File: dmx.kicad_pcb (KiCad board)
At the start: 2 copper layers, 73 x 99.4 mm, 115 parts, among them J1 Conn_01x15_Socket, J10 Conn_01x04_Pin, J11 USB_C_Receptacle_USB2.0_16P, J12 Conn_01x03_Pin, J13 XLR A/B, J14 Conn_01x04_Socket, J15 XLR3, J16 XLR3, J2 Conn_01x04_Pin, J3 Conn_01x15_Socket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

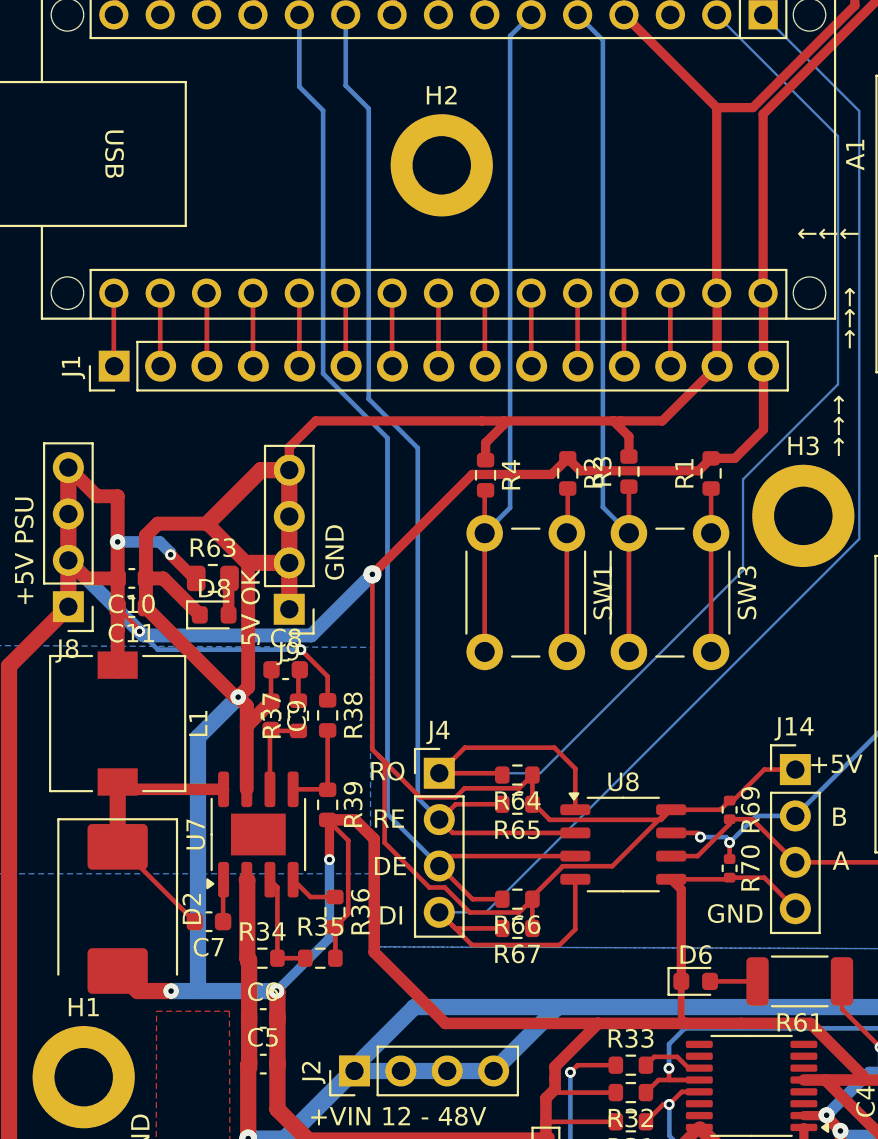
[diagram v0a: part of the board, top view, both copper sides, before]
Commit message: switch to cheaper components.
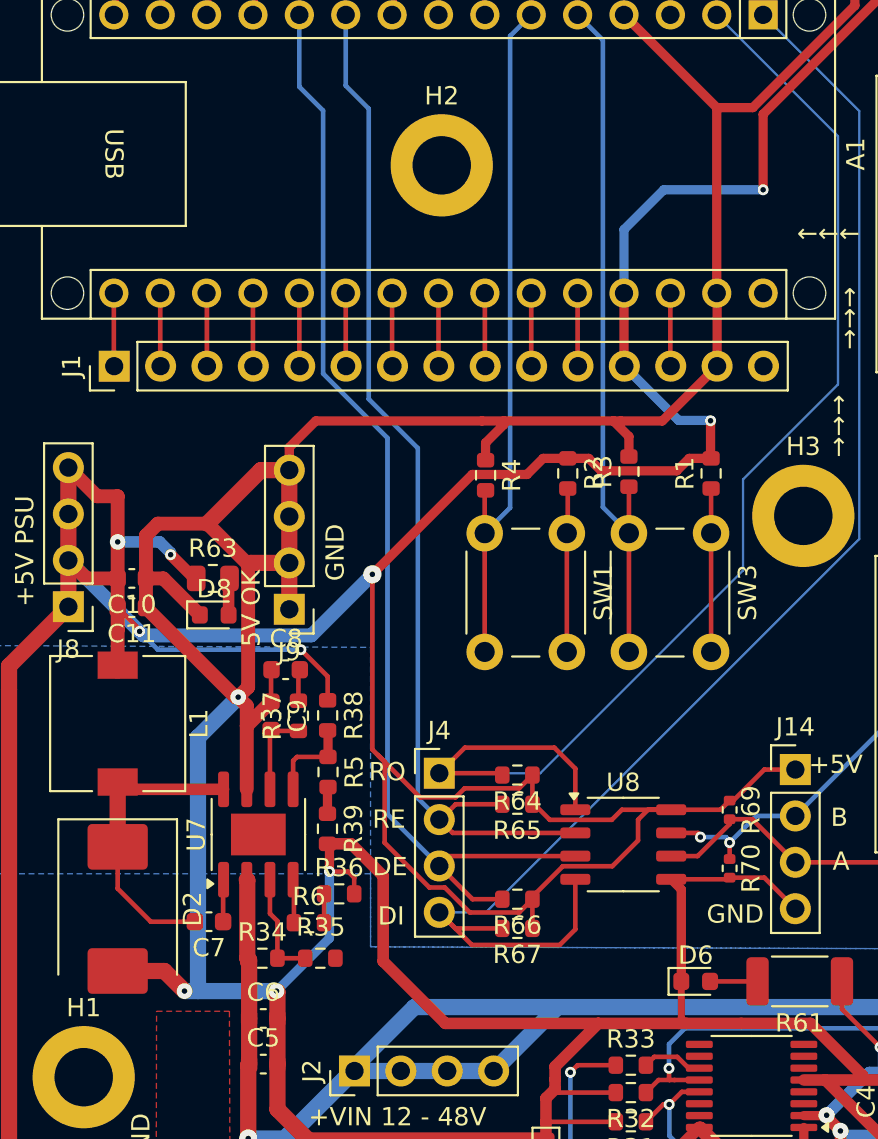
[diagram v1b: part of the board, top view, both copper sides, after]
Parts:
- added R5: 5.1k, Resistor_SMD:R_0603_1608Metric, F.Cu at (109.6, 100.0)
- added R6: 2k, Resistor_SMD:R_0603_1608Metric, F.Cu at (108.5, 108.3)
- R34: value 523k -> 180k
- R35: value 84.5 -> 22k
- R36: value 162k -> 160k
- R39: value 10.2k -> 5.1k
- moved R39 1.31 mm to (109.5, 103.1)
- moved R36 1.03 mm to (110.2, 106.7), turned to 0 degrees
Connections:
- net +VSUB renamed VBUS
- A1 pad 27: Net-(A1-+5V) -> +5VPSU
- A1 pad 30: +5VPSU -> unconnected-(A1-VIN-Pad30)
- J1 pad 12: Net-(A1-+5V) -> +5VPSU
- R36 pad 1: Net-(U7-RT/CLK) -> Net-(R36-Pad1)
- R39 pad 1: Net-(U7-FB) -> Net-(R39-Pad1)
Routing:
- net GND: track 609.7 -> 585.5 mm
- net +5VPSU: track 315.2 -> 323.3 mm, vias 16 -> 18
- net Net-(A1-+5V): track 4.01 -> 0.00 mm
- net Net-(R36-Pad1): track 0.00 -> 1.58 mm
- net Net-(R39-Pad1): track 0.00 -> 1.47 mm
- net Net-(D2-K): track 15.6 -> 16.9 mm

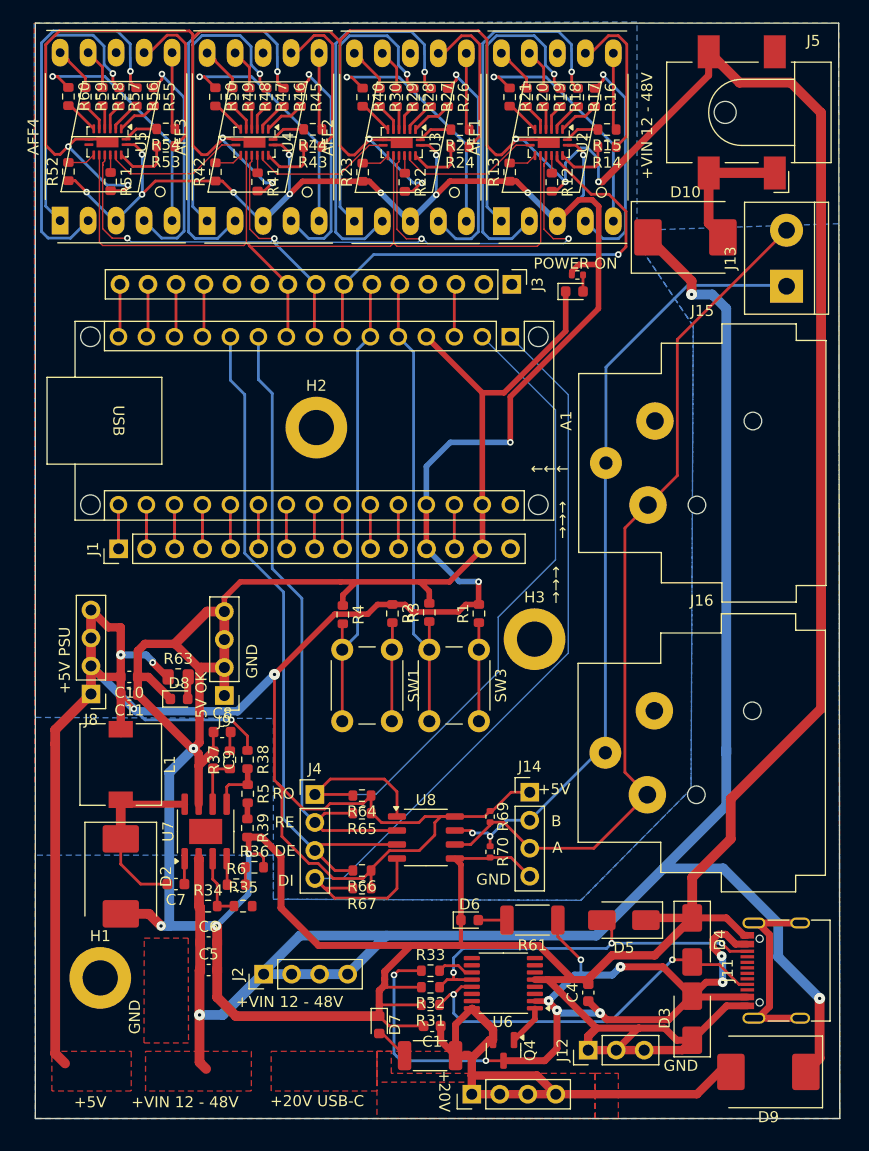
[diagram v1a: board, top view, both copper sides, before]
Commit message: replace extended components with basic components.
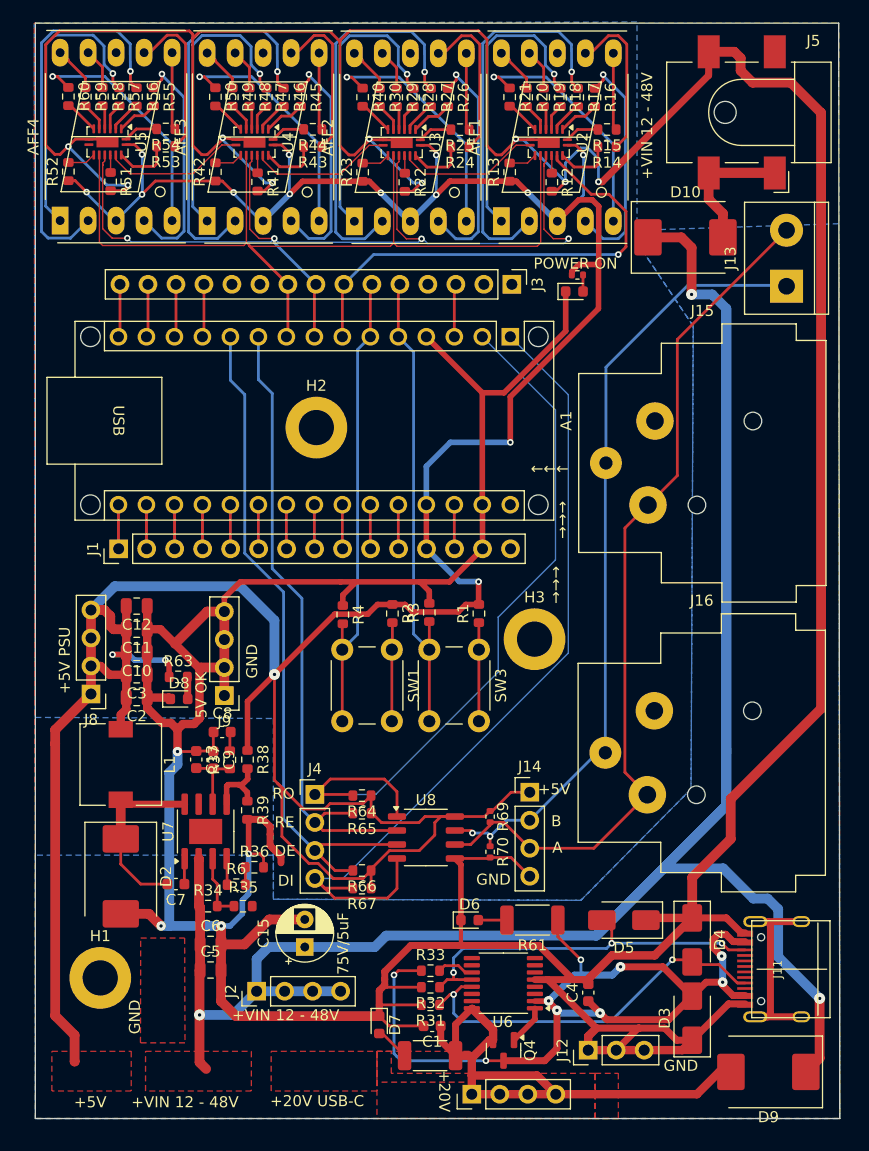
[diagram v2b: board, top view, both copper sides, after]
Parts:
- removed R5: 5.1k, Resistor_SMD:R_0603_1608Metric
- added C12: 10uF, Capacitor_SMD:C_0805_2012Metric, F.Cu at (99.5, 83.0)
- added C13: 22pF, Capacitor_SMD:C_0603_1608Metric, F.Cu at (104.9, 96.9)
- added C15: C_Polarized, Capacitor_THT:CP_Radial_D5.0mm_P2.50mm, F.Cu at (114.8, 113.9)
- added C2: 22uF, Capacitor_SMD:C_0805_2012Metric, F.Cu at (99.5, 91.3)
- added C3: 22uF, Capacitor_SMD:C_0805_2012Metric, F.Cu at (99.5, 89.2)
- C10, C11: value 47uF -> 22uF; footprint Capacitor_SMD:C_0603_1608Metric -> Capacitor_SMD:C_0805_2012Metric
- C5, C6: footprint Capacitor_SMD:C_0603_1608Metric -> Capacitor_SMD:C_0805_2012Metric
- C8: value 6800pF -> 6800pF/6.8nF
- C9: value 39pF -> 18pF
- J11: footprint Connector_USB:USB_C_Receptacle_G-Switch_GT-USB-7010ASV -> USB-C-Power-tester:TYPE-C-31-M-12
- R37: value 13.0k -> 13k
- R38: value 53.6k -> 68k
- R39: value 5.1k -> 13k
- R63: value 200 -> 150; footprint Resistor_SMD:R_0805_2012Metric -> Resistor_SMD:R_0603_1608Metric
- moved C11 5.96 mm to (99.5, 85.1)
- moved C10 2.33 mm to (99.5, 87.2)
- moved J2 1.68 mm to (110.4, 118.0)
- moved R39 1.61 mm to (109.5, 101.5)
- moved J11 1.19 mm to (159.8, 116.0)
- moved C6 0.25 mm to (106.2, 113.7)
- moved C5 0.17 mm to (106.2, 116.0)
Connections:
- R39 pad 1: Net-(R39-Pad1) -> Net-(U7-FB)
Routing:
- net /5Vpsu/+VIN: track 246.8 -> 274.5 mm
- net GND: track 585.5 -> 573.1 mm
- net +5VPSU: track 323.3 -> 327.0 mm, vias 18 -> 16
- net VBUS: track 83.7 -> 81.2 mm
- net Net-(U7-COMP): track 4.80 -> 6.36 mm
- net Net-(U7-FB): track 5.02 -> 6.56 mm
- net Net-(R39-Pad1): track 1.47 -> 0.00 mm
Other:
- board text added: "75V/5uF"

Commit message: add a +5V bridge to disbale the arduino
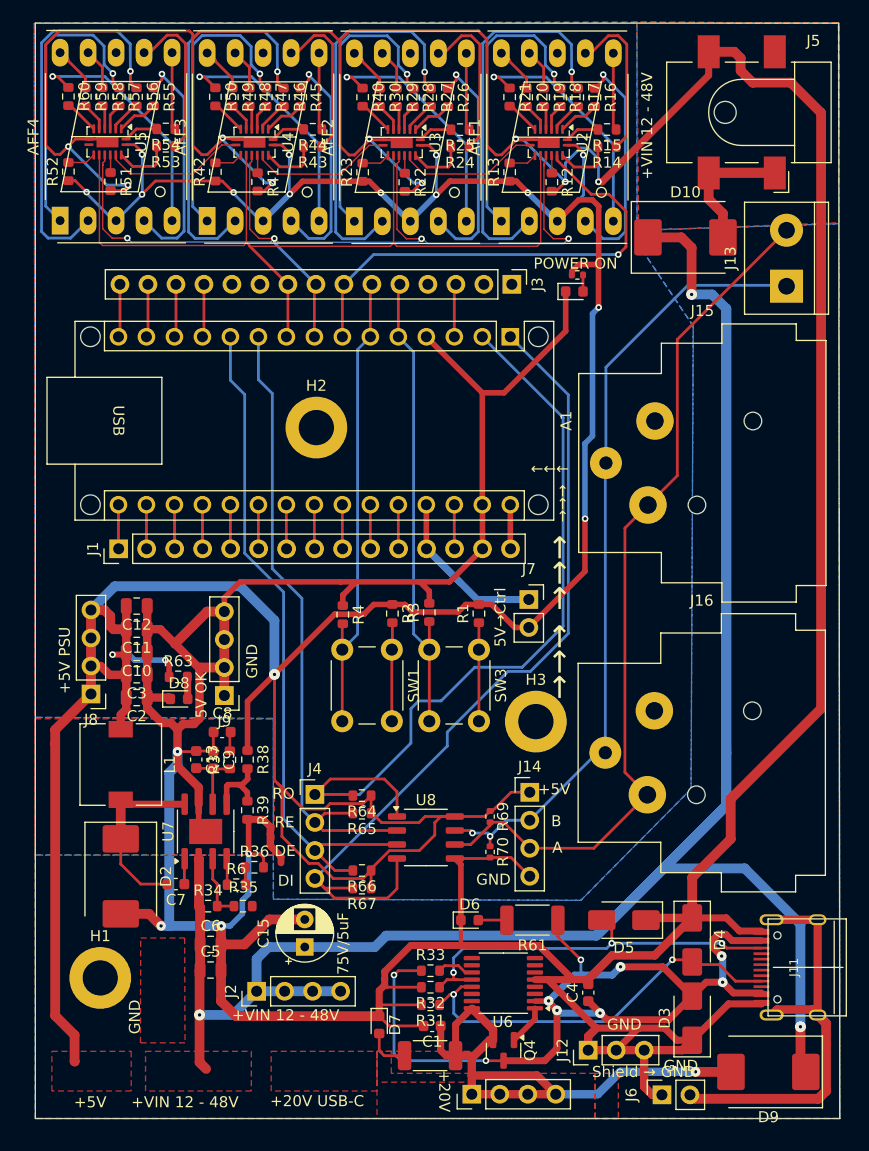
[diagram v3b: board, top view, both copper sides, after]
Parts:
- added J6: Conn_01x02_Socket, Connector_PinSocket_2.54mm:PinSocket_1x02_P2.54mm_Vertical, F.Cu at (147.2, 127.3)
- added J7: Conn_01x02_Socket, Connector_PinSocket_2.54mm:PinSocket_1x02_P2.54mm_Vertical, F.Cu at (135.1, 82.4)
- moved H3 7.48 mm to (135.7, 93.5)
- moved J11 1.49 mm to (161.3, 115.8)
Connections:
- A1 pad 27: +5VPSU -> Net-(A1-+5V)
- A1 pad 30: unconnected-(A1-VIN-Pad30) -> Net-(A1-VIN)
- J1 pad 12: +5VPSU -> Net-(A1-+5V)
- J1 pad 15: +5VPSU -> Net-(A1-VIN)
- J11 pad S1: unconnected-(J11-SHIELD-PadS1) -> Net-(J11-SHIELD)
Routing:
- net Net-(J11-SHIELD): track 0.00 -> 37.8 mm
- net Net-(A1-+5V): track 0.00 -> 19.5 mm
- net unconnected-(J11-SHIELD-PadS1): track 19.4 -> 0.00 mm
- net GND: track 573.1 -> 589.5 mm
- net Net-(A1-VIN): track 0.00 -> 4.04 mm
- net /XLR_TO_UART/RO: track 70.8 -> 74.2 mm
- net VBUS: track 81.2 -> 83.8 mm
- net +5VPSU: track 327.0 -> 324.4 mm
- net Net-(D5-A2): track 34.9 -> 36.3 mm
- net Net-(D4-A2): track 35.3 -> 36.8 mm
- net Net-(D7-A): track 3.13 -> 4.05 mm
- net /5Vpsu/+VIN: track 274.5 -> 273.8 mm
- net /usb-c-pd/+20V: track 52.0 -> 52.5 mm, vias 0 -> 1
- added copper zone on B.Cu, net (none)
- added copper zone on F.Cu, net (none)
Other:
- board text added: "5V→Ctrl"
- board text added: "Shield → GND"

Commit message: change some last parts.
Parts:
- C5, C6: footprint Capacitor_SMD:C_0805_2012Metric -> Capacitor_SMD:C_1206_3216Metric_Pad1.33x1.80mm_HandSolder
- moved C5 0.48 mm to (105.9, 116.4)
- moved C6 0.42 mm to (105.9, 114.0)
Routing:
- net GND: track 589.5 -> 596.7 mm
- net /5Vpsu/+VIN: track 273.8 -> 274.6 mm
